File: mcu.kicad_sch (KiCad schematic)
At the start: 18 parts, among them J33 Conn_ARM_JTAG_SWD_10, SW1 SW_Push, U14 ATSAMD21J18A-A, Y1 Crystal

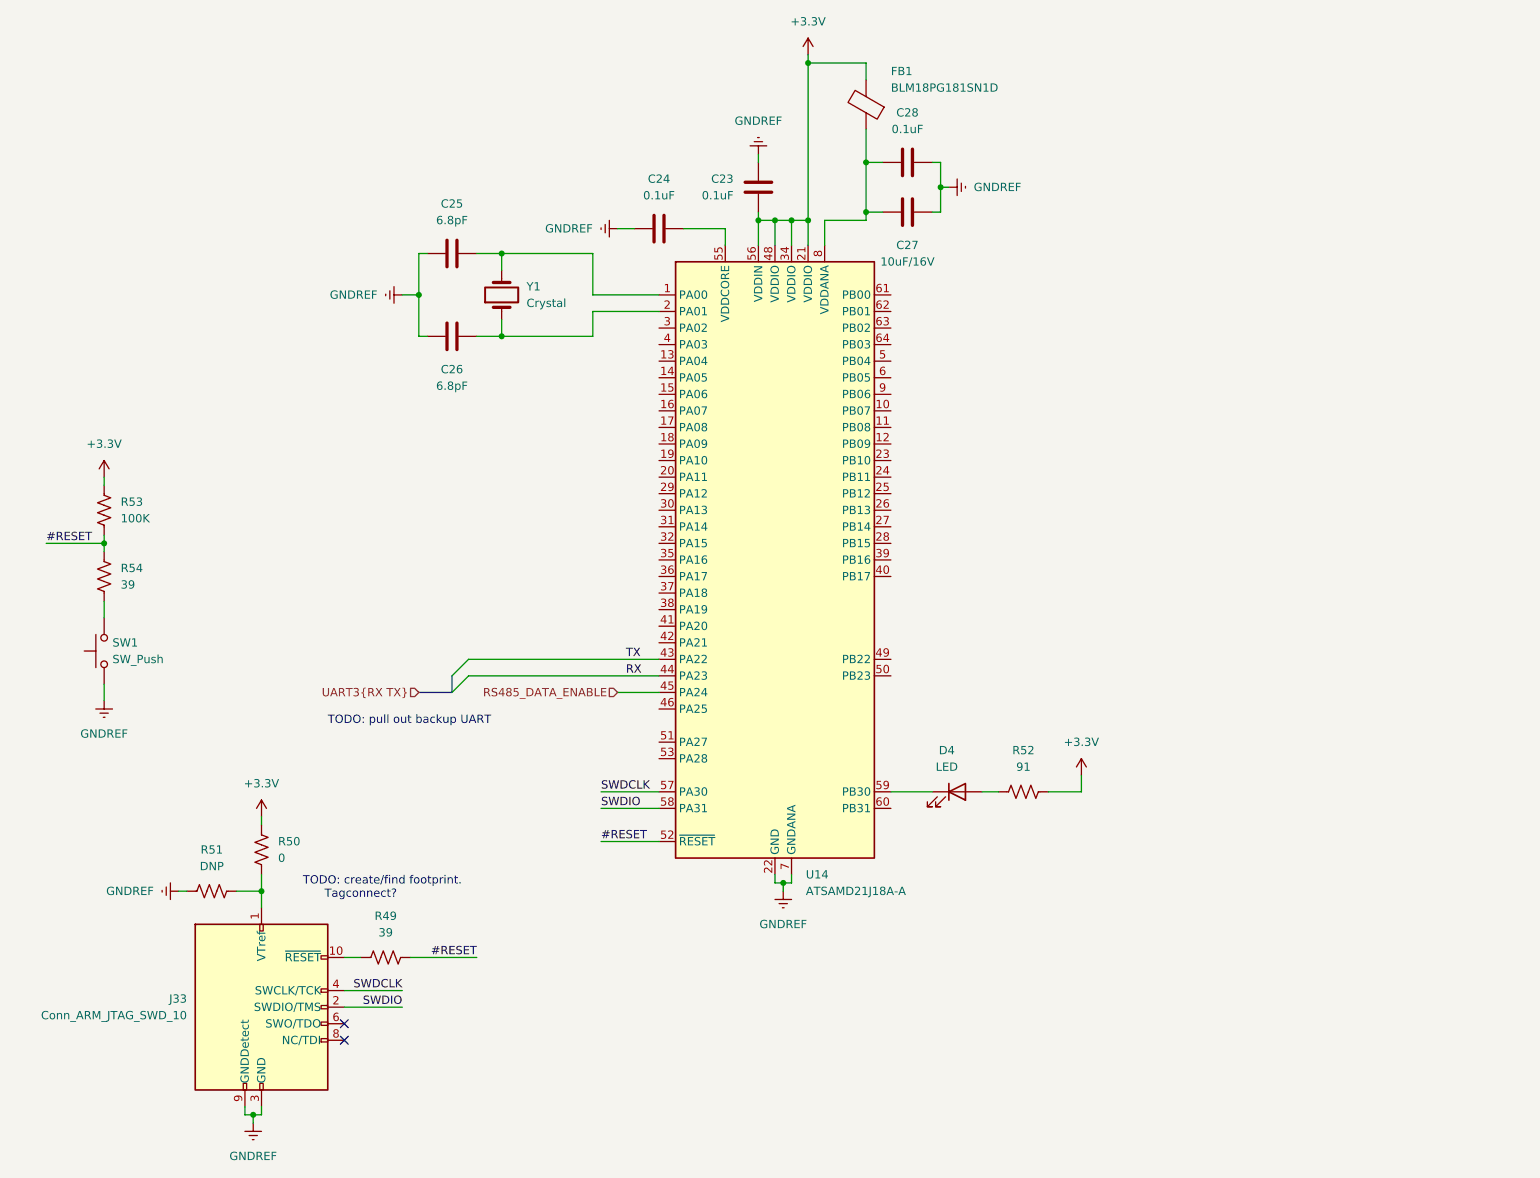
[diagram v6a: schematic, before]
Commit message: add cab signals and connect inputs
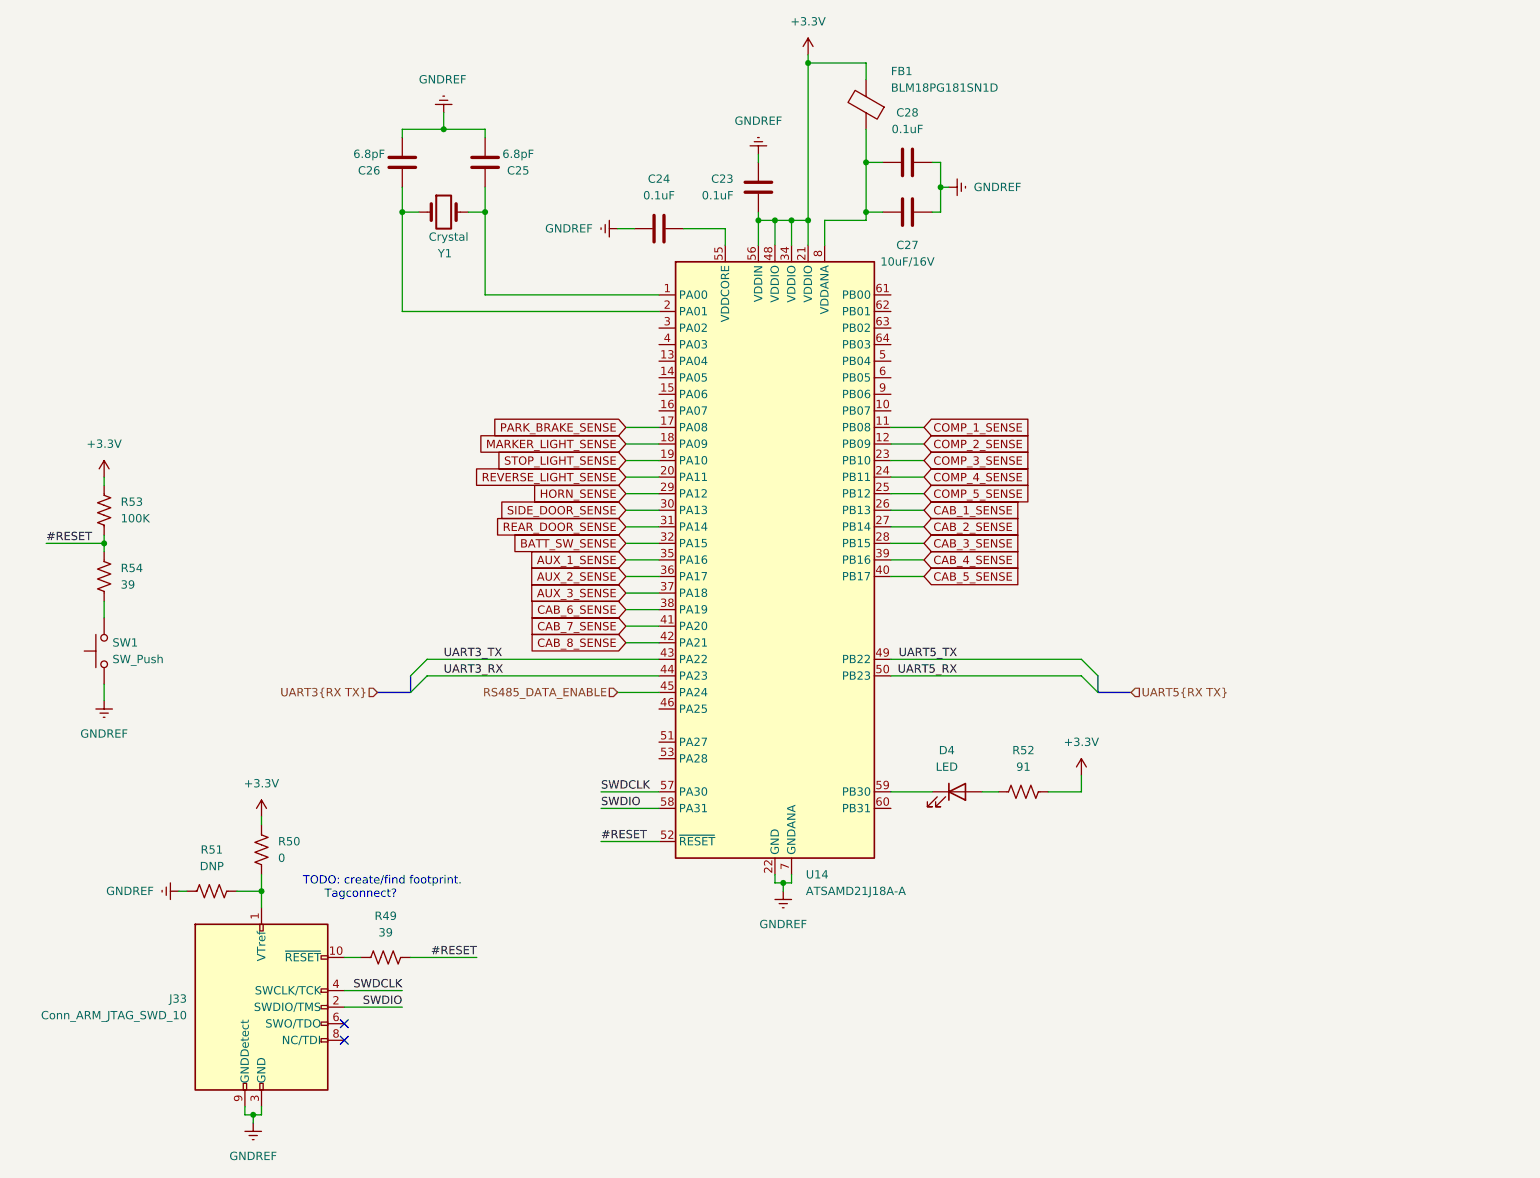
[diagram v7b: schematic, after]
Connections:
- net COMP_1_SENSE: now reaches U14.11 (PB08)
- net COMP_2_SENSE: now reaches U14.12 (PB09)
- net PARK_BRAKE_SENSE: now reaches U14.17 (PA08)
- net MARKER_LIGHT_SENSE: now reaches U14.18 (PA09)
- net STOP_LIGHT_SENSE: now reaches U14.19 (PA10)
- net REVERSE_LIGHT_SENSE: now reaches U14.20 (PA11)
- net COMP_3_SENSE: now reaches U14.23 (PB10)
- net COMP_4_SENSE: now reaches U14.24 (PB11)
- net COMP_5_SENSE: now reaches U14.25 (PB12)
- net CAB_1_SENSE: now reaches U14.26 (PB13)
- net CAB_2_SENSE: now reaches U14.27 (PB14)
- net CAB_3_SENSE: now reaches U14.28 (PB15)
- net HORN_SENSE: now reaches U14.29 (PA12)
- net SIDE_DOOR_SENSE: now reaches U14.30 (PA13)
- net REAR_DOOR_SENSE: now reaches U14.31 (PA14)
- net BATT_SW_SENSE: now reaches U14.32 (PA15)
- net AUX_1_SENSE: now reaches U14.35 (PA16)
- net AUX_2_SENSE: now reaches U14.36 (PA17)
- net AUX_3_SENSE: now reaches U14.37 (PA18)
- net CAB_6_SENSE: now reaches U14.38 (PA19)
- net CAB_4_SENSE: now reaches U14.39 (PB16)
- net CAB_5_SENSE: now reaches U14.40 (PB17)
- net CAB_7_SENSE: now reaches U14.41 (PA20)
- net CAB_8_SENSE: now reaches U14.42 (PA21)
- net UART5_TX: now reaches U14.49 (PB22)
- net UART5_RX: now reaches U14.50 (PB23)
- net RX renamed UART3_RX
- net TX renamed UART3_TX
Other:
- note removed: "TODO: pull out backup UART"
- moved on the sheet: C25, C26, Y1

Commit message: connect signals to connectors, start layout
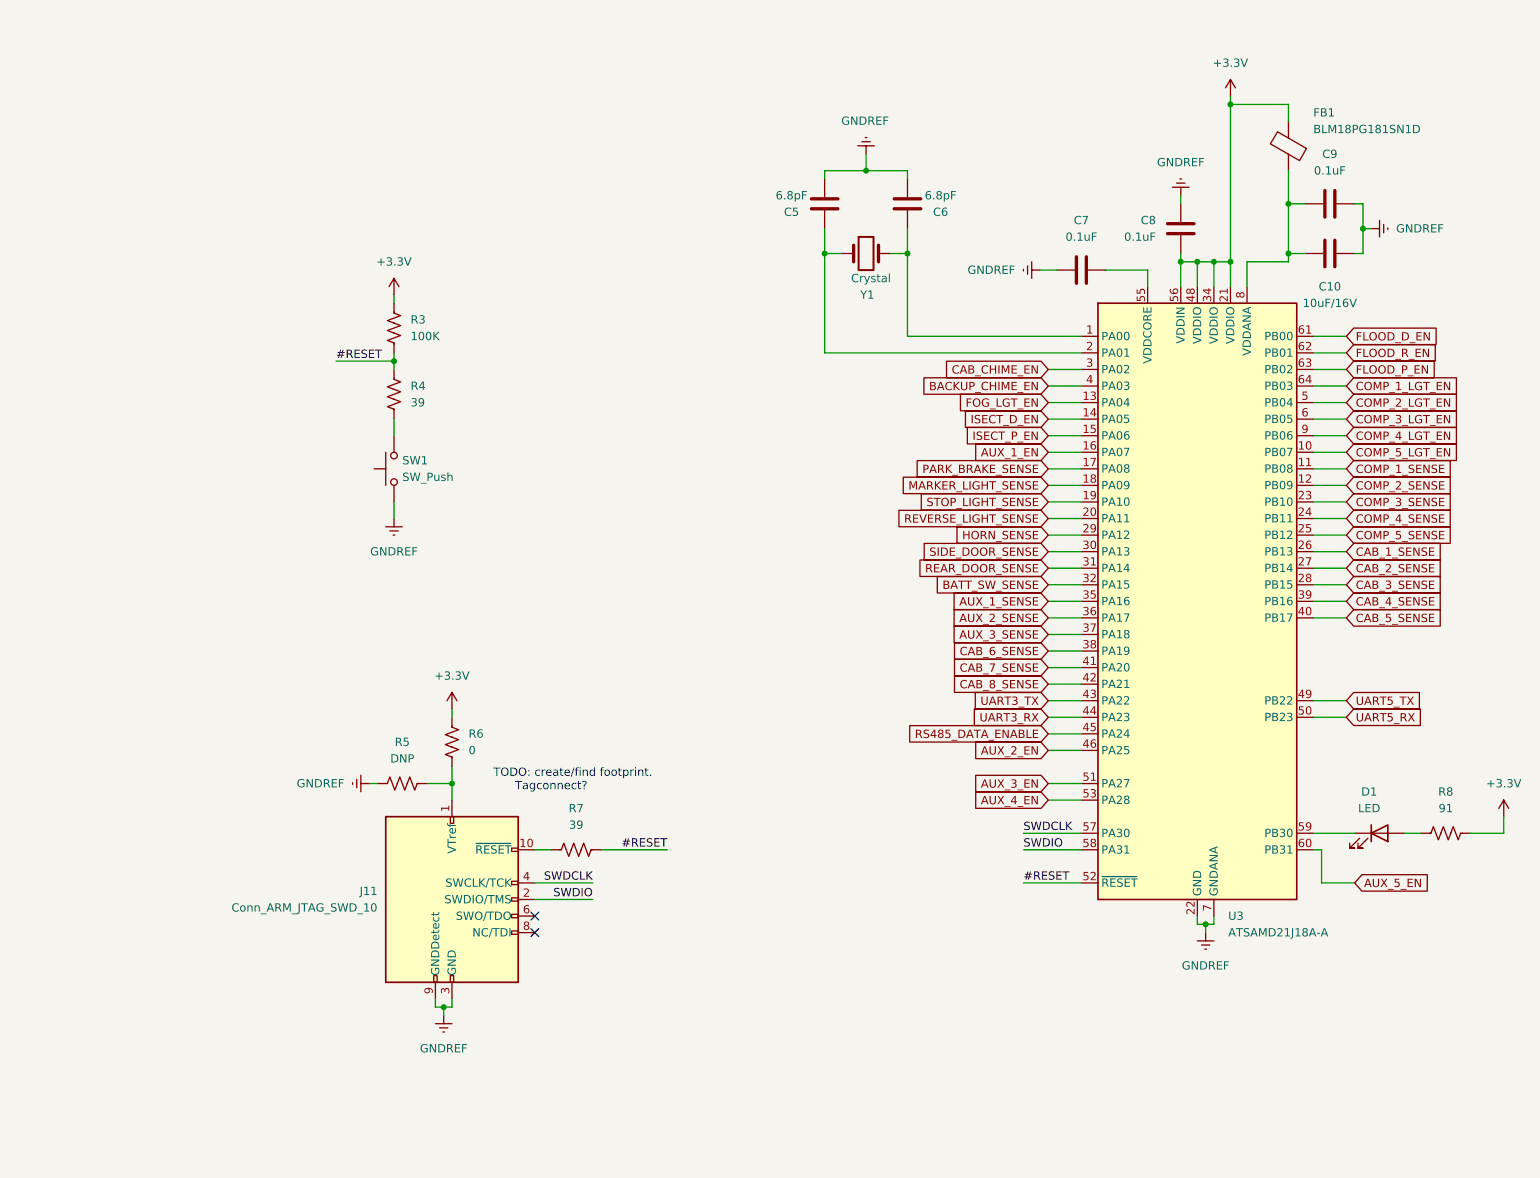
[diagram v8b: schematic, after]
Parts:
- renumbered C27 to C10, C26 to C5, C25 to C6, C24 to C7, C23 to C8, C28 to C9, D4 to D1, J33 to J11, R53 to R3, R54 to R4, R51 to R5, R50 to R6, R49 to R7, R52 to R8, U14 to U3
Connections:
- net COMP_5_LGT_EN: now reaches U3.10 (PB07)
- net FOG_LGT_EN: now reaches U3.13 (PA04)
- net ISECT_D_EN: now reaches U3.14 (PA05)
- net ISECT_P_EN: now reaches U3.15 (PA06)
- net AUX_1_EN: now reaches U3.16 (PA07)
- net CAB_CHIME_EN: now reaches U3.3 (PA02)
- net BACKUP_CHIME_EN: now reaches U3.4 (PA03)
- net AUX_2_EN: now reaches U3.46 (PA25)
- net COMP_2_LGT_EN: now reaches U3.5 (PB04)
- net AUX_3_EN: now reaches U3.51 (PA27)
- net AUX_4_EN: now reaches U3.53 (PA28)
- net COMP_3_LGT_EN: now reaches U3.6 (PB05)
- net AUX_5_EN: now reaches U3.60 (PB31)
- net FLOOD_D_EN: now reaches U3.61 (PB00)
- net FLOOD_R_EN: now reaches U3.62 (PB01)
- net FLOOD_P_EN: now reaches U3.63 (PB02)
- net COMP_1_LGT_EN: now reaches U3.64 (PB03)
- net COMP_4_LGT_EN: now reaches U3.9 (PB06)
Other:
- moved on the sheet: C10, C5, C6, C7, C8, C9, D1, FB1, J11, R3, R4, R5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
